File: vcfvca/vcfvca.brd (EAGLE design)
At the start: 160 x 100 mm, 104 parts, among them IC1 LM13700N, IC2 LM4558N, IC3 LM13700N, IC4 LM13700N, IC5 LM4558N, J1 POWER, J2 FREQ, J3 RES, J4 AMP, J5 AUD_IN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

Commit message: Start board placement
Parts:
- moved R35 202.5 mm to (99.1, 27.9), turned to 90 degrees
- moved R28 200.7 mm to (104.1, 57.1), turned to 90 degrees
- moved R34 186.8 mm to (95.2, 27.9), turned to 270 degrees
- moved R27 184.3 mm to (100.3, 57.1), turned to 90 degrees
- moved C20 174.9 mm to (121.9, 29.2)
- moved IC4 174.1 mm to (102.9, 41.9)
- moved S1 172.9 mm to (82.5, 14.0), turned to 180 degrees
- moved R33 171.1 mm to (91.4, 27.9), turned to 90 degrees
- moved R26 167.9 mm to (96.5, 57.1), turned to 270 degrees
- moved R13 167.9 mm to (80.0, 27.9), turned to 90 degrees
- moved C19 167.0 mm to (121.9, 21.6)
- moved Q2 164.1 mm to (74.9, 22.9), turned to 270 degrees
- moved Q6 159.5 mm to (71.1, 61.0), turned to 90 degrees
- moved R21 154.8 mm to (58.4, 55.9), turned to 90 degrees
- moved VR2 151.2 mm to (105.4, 10.2)
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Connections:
- net GND: now also IC4.14, IC4.4; no longer IC4.13, IC4.3
- net N$10: now also IC3.1; no longer IC1.16
- net N$11: now also IC3.3; no longer IC1.14
- net N$12: now also IC3.4; no longer IC1.13
- net N$14: now also IC1.14; no longer IC3.3
- net N$15: now also IC1.13; no longer IC3.4
- net N$16: now also IC4.13; no longer IC4.4
- net N$2: now also IC3.5; no longer IC1.12
- net N$22: now also IC4.16; no longer IC4.1
- net N$23: now also IC1.16; no longer IC3.1
- net N$25: now also IC4.12; no longer IC4.5
- net N$30: now also IC4.3; no longer IC4.14
- net N$31: now also IC4.5; no longer IC4.12
- net N$33: now also IC4.1; no longer IC4.16
- net N$4: now also IC1.12; no longer IC3.5
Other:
- board size 160 x 100 mm -> 160 x 154.6 mm

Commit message: Done placement
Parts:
- moved R49 257.0 mm to (148.6, 14.0), turned to 90 degrees
- moved C15 249.2 mm to (156.2, 26.7), turned to 270 degrees
- moved J4 241.8 mm to (156.2, 14.0), turned to 90 degrees
- moved C14 225.1 mm to (141.0, 26.7), turned to 270 degrees
- moved C10 220.8 mm to (149.9, 38.1), turned to 90 degrees
- moved R53 219.6 mm to (144.8, 14.0), turned to 90 degrees
- moved J6 213.5 mm to (156.2, 36.8), turned to 90 degrees
- moved C9 203.2 mm to (146.1, 36.8), turned to 270 degrees
- moved Q10 201.8 mm to (137.2, 15.2), turned to 90 degrees
- moved IC2 195.4 mm to (148.6, 26.7)
- moved R38 193.5 mm to (142.2, 39.4), turned to 90 degrees
- moved VR8 192.2 mm to (144.8, 3.81)
- moved VR5 188.0 mm to (111.8, 8.89), turned to 180 degrees
- moved R50 181.8 mm to (141.0, 14.0), turned to 270 degrees
- moved R37 177.6 mm to (138.4, 39.4), turned to 270 degrees
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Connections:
- net GND: now also IC4.13, IC4.3; no longer IC4.14, IC4.4
- net N$16: now also IC4.4; no longer IC4.13
- net N$22: now also IC4.1; no longer IC4.16
- net N$25: now also IC4.5; no longer IC4.12
- net N$30: now also IC4.14; no longer IC4.3
- net N$31: now also IC2.6, IC4.12; no longer IC2.2, IC4.5
- net N$33: now also IC4.16; no longer IC4.1
- net N$35: now also IC2.7; no longer IC2.1
- net N$50: now also IC2.1; no longer IC2.7
- net N$52: now also IC2.2; no longer IC2.6
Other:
- board size 160 x 154.6 mm -> 160 x 50.5 mm

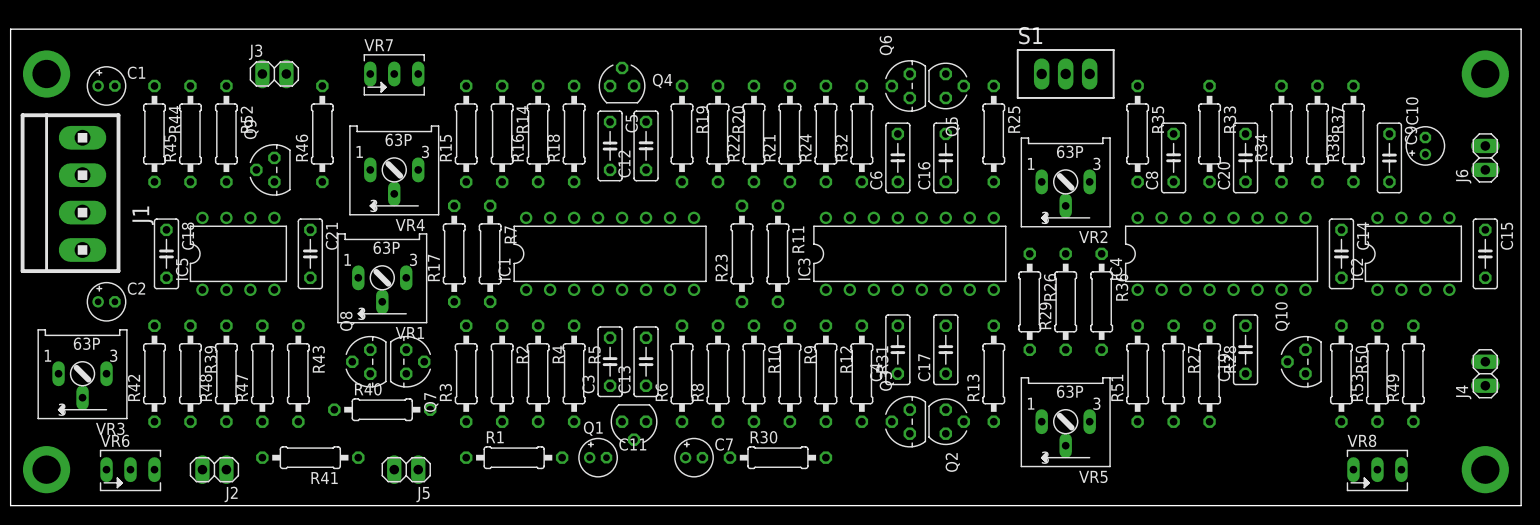
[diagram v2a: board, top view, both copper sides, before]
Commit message: Routed the signals
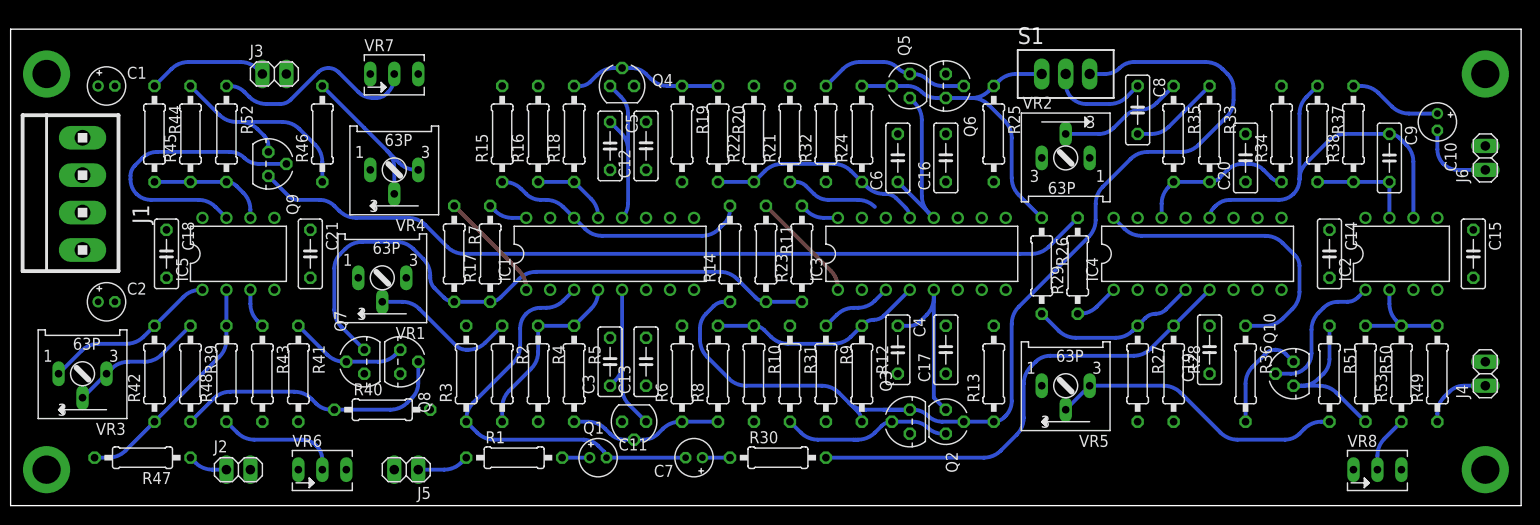
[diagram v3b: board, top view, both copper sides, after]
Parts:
- moved R14 27.3 mm to (76.2, 26.7), turned to 90 degrees
- moved VR6 20.3 mm to (33.0, 3.81)
- moved R51 20.3 mm to (139.7, 14.0), turned to 270 degrees
- moved R36 17.0 mm to (130.8, 14.0)
- moved R47 15.5 mm to (14.0, 5.08), turned to 180 degrees
- moved R41 8.98 mm to (30.5, 14.0), turned to 270 degrees
- moved R31 7.62 mm to (82.5, 14.0)
- moved C8 6.35 mm to (119.4, 41.9), turned to 270 degrees
- moved R23 6.35 mm to (83.8, 26.7)
- moved Q7 4.44 mm to (37.5, 15.2), turned to 90 degrees
- moved R26 4.02 mm to (109.2, 25.4)
- moved R29 4.02 mm to (113.0, 25.4)
- moved C19 3.81 mm to (127.0, 16.5)
- moved Q5 3.81 mm to (95.2, 44.5), turned to 90 degrees
- moved Q6 3.81 mm to (99.1, 44.5), turned to 270 degrees
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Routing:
- net N$18: track 0.00 -> 110.7 mm
- net I_RES: track 0.00 -> 89.8 mm
- net I_FREQ: track 0.00 -> 66.1 mm
- net N$25: track 0.00 -> 50.6 mm
- net N$9: track 0.00 -> 44.1 mm
- net N$31: track 0.00 -> 44.0 mm
- net N$19: track 0.00 -> 35.9 mm
- net N$33: track 0.00 -> 32.0 mm
- net N$45: track 0.00 -> 31.5 mm
- net N$47: track 0.00 -> 30.3 mm
- net N$40: track 0.00 -> 29.4 mm
- net N$14: track 0.00 -> 27.6 mm
- net N$42: track 0.00 -> 24.7 mm
- net N$46: track 0.00 -> 24.3 mm
- net N$20: track 0.00 -> 23.2 mm
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
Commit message: Finsihed routing!
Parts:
- moved R31 30.4 mm to (111.8, 5.71), turned to 180 degrees
- moved R41 14.0 mm to (44.5, 14.0), turned to 90 degrees
- moved Q7 3.81 mm to (33.7, 15.2)
- moved Q8 3.81 mm to (37.5, 15.2)
- moved R40 3.81 mm to (35.6, 10.2)
- moved R10 2.54 mm to (81.3, 14.0)
- moved R22 1.27 mm to (78.7, 40.6)
- moved R8 1.27 mm to (76.2, 14.0)
- turned C1 to 180 degrees
- turned R11 to 90 degrees
- turned R7 to 90 degrees
- turned VR1 to 0 degrees
- turned VR2 to 180 degrees
- turned VR6 to 180 degrees
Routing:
- net GND: track 0.00 -> 674.9 mm
- net +15V: track 0.00 -> 444.9 mm, vias 0 -> 2
- net -15V: track 0.00 -> 292.0 mm, vias 0 -> 1
- net I_FREQ: track 66.1 -> 83.2 mm
- net I_RES: track 89.8 -> 104.0 mm
- net N$25: track 50.6 -> 57.1 mm
- net N$43: track 12.6 -> 18.9 mm
- net N$32: track 13.1 -> 18.4 mm
- net N$27: track 17.9 -> 14.1 mm
- net N$35: track 11.4 -> 15.2 mm
- net N$48: track 12.6 -> 16.4 mm
- net N$40: track 29.4 -> 25.6 mm
- net N$34: track 15.4 -> 19.2 mm
- net N$7: track 11.9 -> 8.80 mm
- net N$10: track 11.9 -> 9.37 mm
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
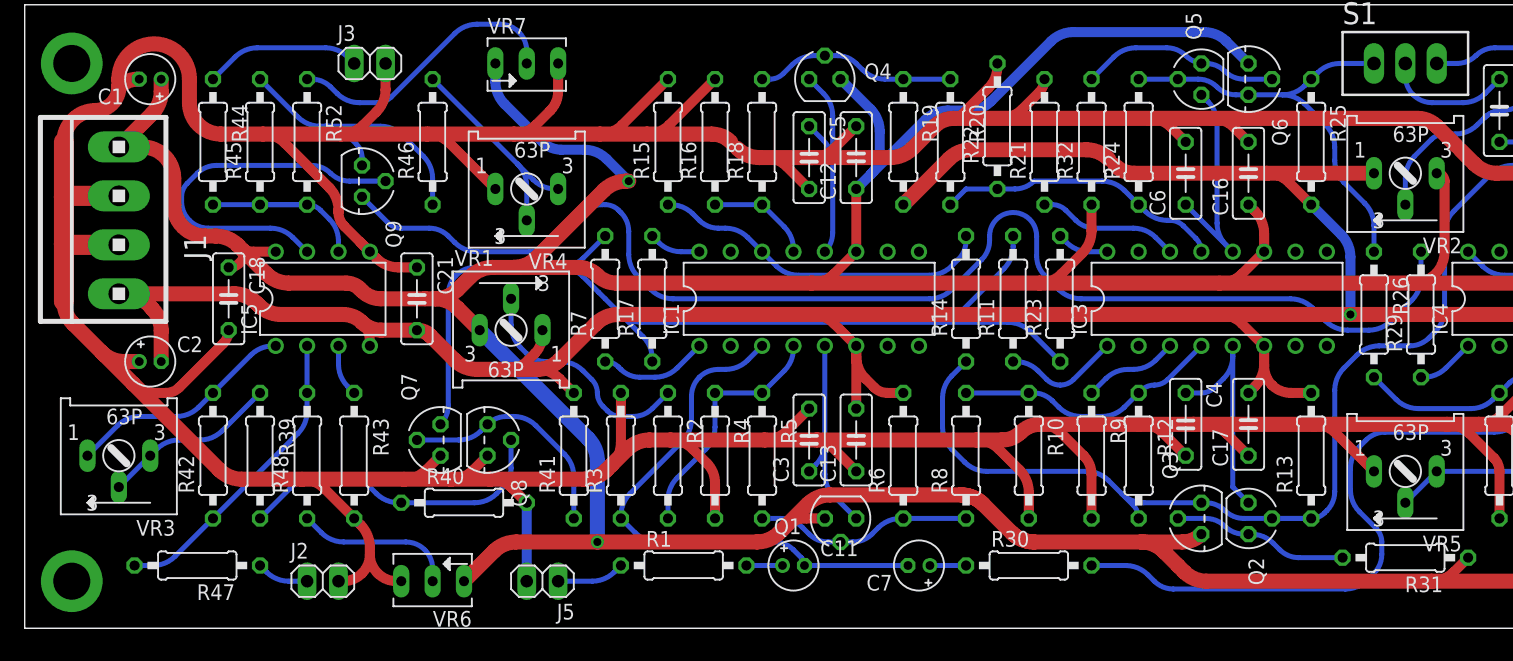
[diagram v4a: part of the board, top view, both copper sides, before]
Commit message: Clear DRC errors
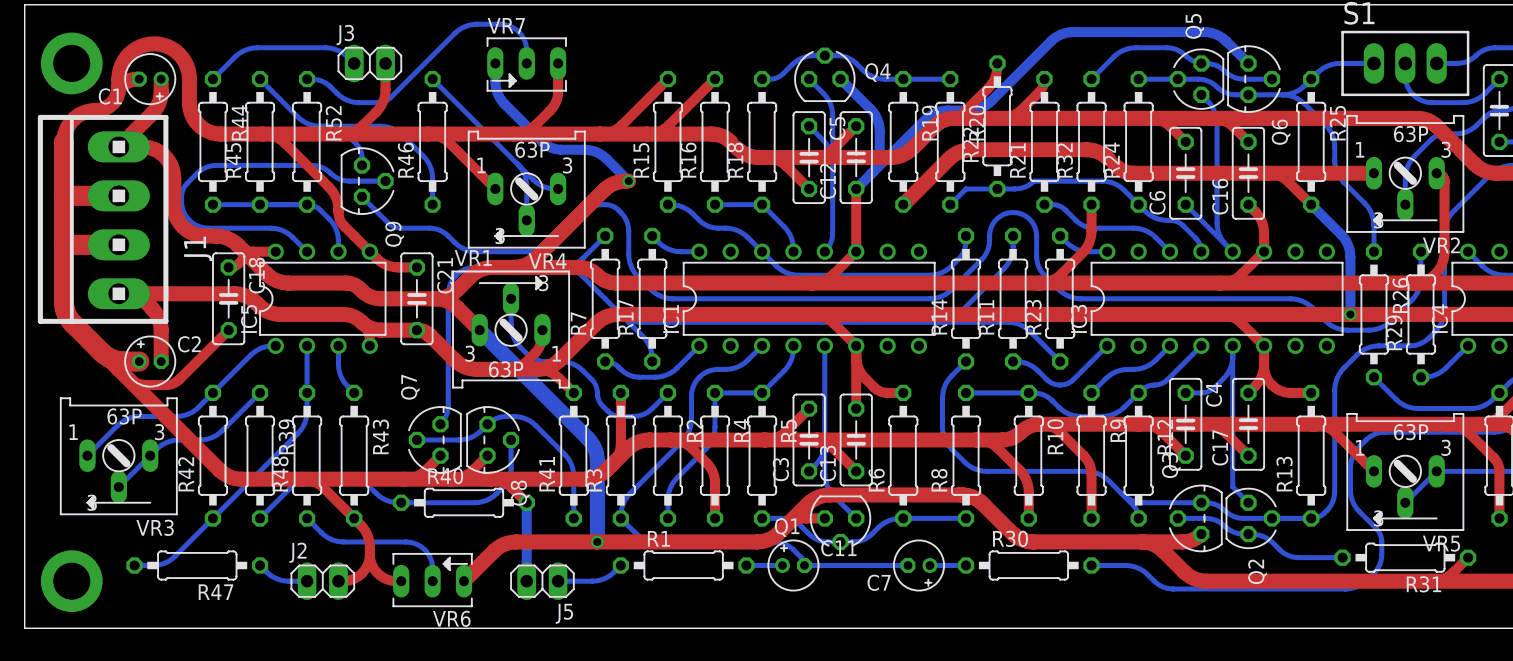
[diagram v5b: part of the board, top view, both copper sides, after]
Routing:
- net +15V: track 444.9 -> 439.2 mm
- net GND: track 674.9 -> 671.8 mm
